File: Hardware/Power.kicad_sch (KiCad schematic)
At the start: 0 parts

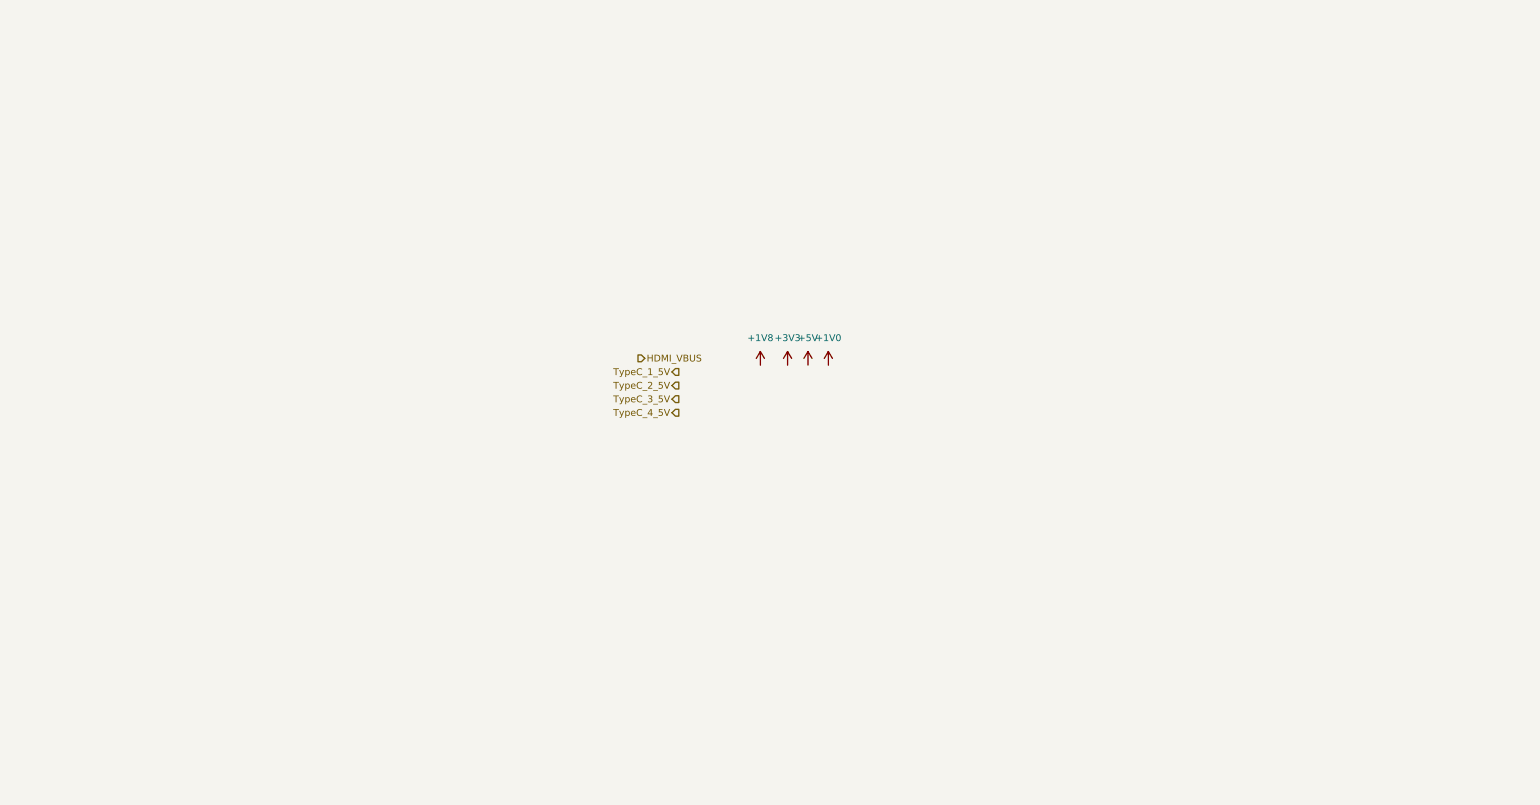
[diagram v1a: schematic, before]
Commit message: 完成除MCU外的设计
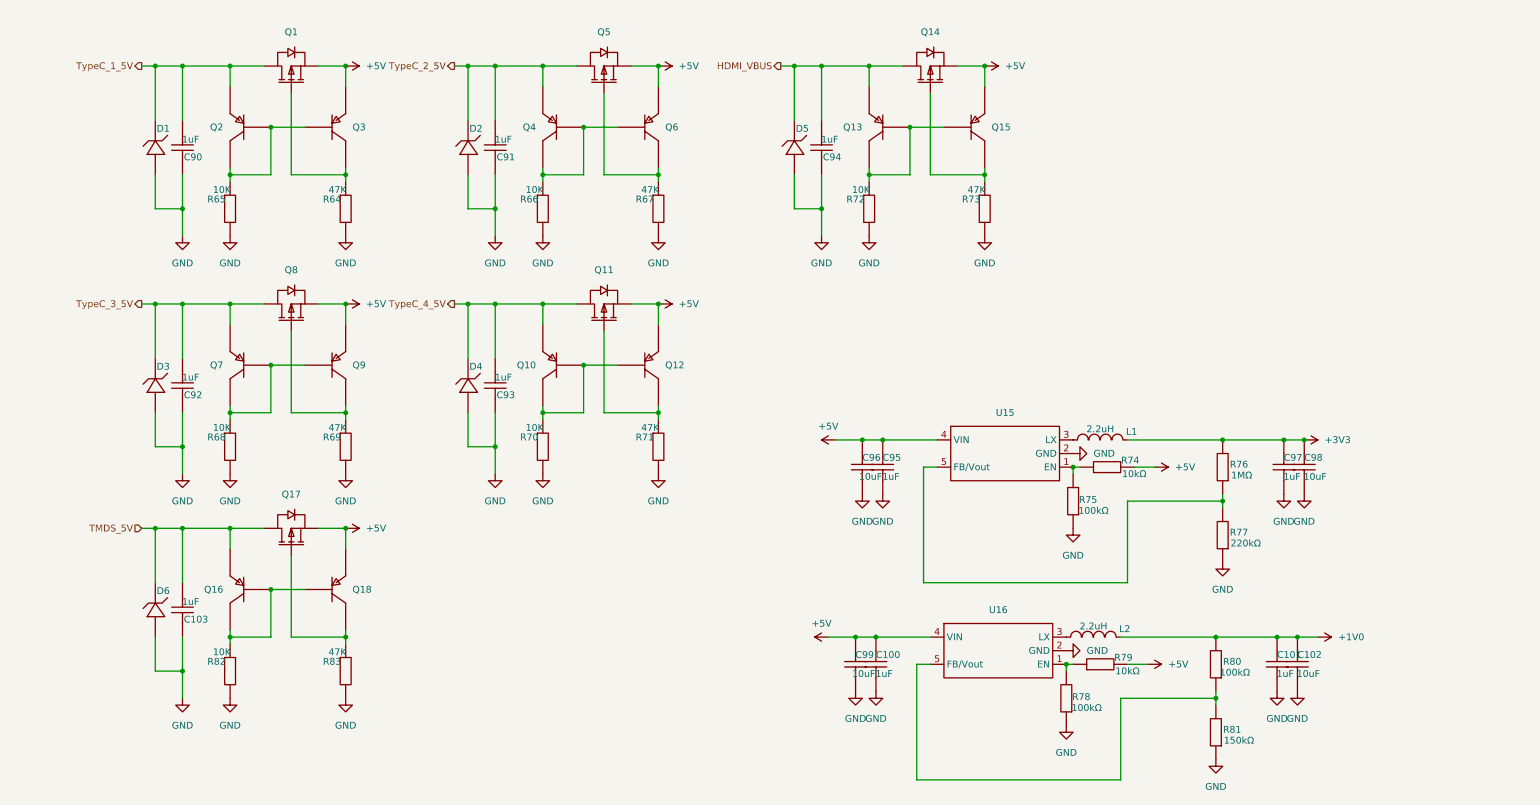
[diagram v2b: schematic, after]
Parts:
- added C100, C101, C103, C90, C91, C92, C93, C94, C95, C97: 1uF, persional_library:C0603, symbol persional_library:C0603
- added C102, C96, C98, C99: 10uF, persional_library:C0603, symbol persional_library:C0603
- added D1, D2, D3, D4, D5, D6: ~, persional_library:SMB_L4.6-W3.6-LS5.3-RD, symbol persional_library:TVS_Diode_SMBJ5.0A
- added L1, L2: 2.2uH, persional_library:IND-SMD_L7.0-W6.6, symbol persional_library:L0630-2.2UH
- added Q1, Q11, Q14, Q17, Q5, Q8: ~, persional_library:SOT-23-3_L2.9-W1.3-P0.95-LS2.4-BR-1, symbol persional_library:MOSFET_DMG2305UX
- added Q10, Q12, Q13, Q15, Q16, Q18, Q2, Q3, Q4, Q6, Q7, Q9: ~, persional_library:SOT-23-3_L2.9-W1.3-P1.90-LS2.4-BR, symbol persional_library:Transistor_PNP_MMBT4403LT1G
- added R64, R67, R69, R71, R73, R83: 47K, persional_library:R0603, symbol persional_library:R0603
- added R65, R66, R68, R70, R72, R82: 10K, persional_library:R0603, symbol persional_library:R0603
- added R74, R79: 10kΩ, persional_library:R0603, symbol persional_library:R0603
- added R75, R78, R80: 100kΩ, persional_library:R0603, symbol persional_library:R0603
- added R76: 1MΩ, persional_library:R0603, symbol persional_library:R0603
- added R77: 220kΩ, persional_library:R0603, symbol persional_library:R0603
- added R81: 150kΩ, persional_library:R0603, symbol persional_library:R0603
- added U15, U16: ~, persional_library:SOT-23-5_L3.0-W1.7-P0.95-LS2.8-BR, symbol persional_library:DCDC-LP3220AB5F
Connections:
- net +1V0: now also C101.2, C102.2, L2.2, R80.2
- net +3V3: now also C97.2, C98.2, L1.2, R76.2
- net +5V: now also C100.2, C95.2, C96.2, C99.2, Q1.2 (S), Q11.2 (S), Q12.2 (E), Q14.2 (S), Q15.2 (E), Q17.2 (S), Q18.2 (E), Q3.2 (E), Q5.2 (S), Q6.2 (E), Q8.2 (S), Q9.2 (E), R74.2, R79.2, U15.4 (VIN), U16.4 (VIN)
- net HDMI_VBUS: now also C94.2, D5.1, Q13.2 (E), Q14.3 (D)
- net TypeC_1_5V: now also C90.2, D1.1, Q1.3 (D), Q2.2 (E)
- net TypeC_2_5V: now also C91.2, D2.1, Q4.2 (E), Q5.3 (D)
- net TypeC_3_5V: now also C92.2, D3.1, Q7.2 (E), Q8.3 (D)
- net TypeC_4_5V: now also C93.2, D4.1, Q10.2 (E), Q11.3 (D)
- new net: Q5.1 (G), Q6.3 (C), R67.1
- new net: Q2.1 (B), Q2.3 (C), Q3.1 (B), R65.1
- new net: Q4.1 (B), Q4.3 (C), Q6.1 (B), R66.1
- new net: Q1.1 (G), Q3.3 (C), R64.1
- new net: Q13.1 (B), Q13.3 (C), Q15.1 (B), R72.1
- new net: Q10.1 (B), Q10.3 (C), Q12.1 (B), R70.1
- new net: R76.1, R77.2, U15.5 (FB/Vout)
- new net: R74.1, R75.2, U15.1 (EN)
- new net: Q16.1 (B), Q16.3 (C), Q18.1 (B), R82.1
- new net: Q11.1 (G), Q12.3 (C), R71.1
- new net: L1.1, U15.3 (LX)
- new net: Q17.1 (G), Q18.3 (C), R83.1
- new net: R78.2, R79.1, U16.1 (EN)
- new net: L2.1, U16.3 (LX)
- new net: R80.1, R81.2, U16.5 (FB/Vout)
- new net: Q14.1 (G), Q15.3 (C), R73.1
- new net: Q7.1 (B), Q7.3 (C), Q9.1 (B), R68.1
- new net: Q8.1 (G), Q9.3 (C), R69.1
- new net GND: C100.1, C101.1, C102.1, C103.1, C90.1, C91.1, C92.1, C93.1, C94.1, C95.1, C96.1, C97.1, C98.1, C99.1, D1.2, D2.2, D3.2, D4.2, D5.2, D6.2, R64.2, R65.2, R66.2, R67.2, R68.2, R69.2, R70.2, R71.2, R72.2, R73.2, R75.1, R77.1, R78.1, R81.1, R82.2, R83.2, U15.2 (GND), U16.2 (GND)
- new net TMDS_5V: C103.2, D6.1, Q16.2 (E), Q17.3 (D)

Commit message: 修改了电源供电部分的内容
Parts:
- removed C102: 10uF, persional_library:C0603, symbol persional_library:C0603
- removed R78, R80: 100kΩ, persional_library:R0603, symbol persional_library:R0603
- removed R79: 10kΩ, persional_library:R0603, symbol persional_library:R0603
- removed R81: 150kΩ, persional_library:R0603, symbol persional_library:R0603
- removed U15, U16: ~, persional_library:SOT-23-5_L3.0-W1.7-P0.95-LS2.8-BR, symbol persional_library:DCDC-LP3220AB5F
- added U15: ~, persional_library:TSOT-23-8_L2.9-W1.6-P0.65-LS2.8-BL, symbol persional_library:DCDC_MP2122AGJ-Z
- added U16: ~, persional_library:SOT-223-4_L6.5-W3.5-P2.30-LS7.0-BR, symbol persional_library:LDO_AMS1117-3.3
- C100, C97: value 1uF -> 10uF
- C101, C95: value 1uF -> 100nF
- R74: value 10kΩ -> 150K
- R75: value 100kΩ -> 150K
- R76: value 1MΩ -> 680K
- R77: value 220kΩ -> 100K
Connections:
- net +1V0: now also C98.2, R77.2; no longer C101.2
- net +3V3: no longer C98.2
- net +5V: now also U15.2 (EN2), U15.4 (EN1), U15.7 (IN), U16.3 (VIN); no longer C100.2, R74.2
- net GND: now also R74.2, R75.2, U15.5 (GND), U16.1 (ADJ(GND)); no longer R75.1, R77.1
- net at R76.1: now also R75.1, U15.8 (FB1); no longer R77.2
- net at R74.1: now also R77.1, U15.1 (FB2); no longer R75.2
- net at L1.1: now also U15.6 (SW1)
- net at L2.1: now also U15.3 (SW2)
- new net +3.3V: C100.2, C101.2, U16.2 (VOUT(TAB)), U16.4 (TAB)

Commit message: complete sch
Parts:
- added F1, F2, F3, F4, F5, F6: ~, persional_library:F1206, symbol persional_library:F1206
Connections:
- net HDMI_VBUS: now also F6.1; no longer C94.2, D5.1, Q13.2 (E), Q14.3 (D)
- net TMDS_5V: now also F3.1; no longer C103.2, D6.1, Q16.2 (E), Q17.3 (D)
- net TypeC_1_5V: now also F1.1; no longer C90.2, D1.1, Q1.3 (D), Q2.2 (E)
- net TypeC_2_5V: now also F5.1; no longer C91.2, D2.1, Q4.2 (E), Q5.3 (D)
- net TypeC_3_5V: now also F2.1; no longer C92.2, D3.1, Q7.2 (E), Q8.3 (D)
- net TypeC_4_5V: now also F4.1; no longer C93.2, D4.1, Q10.2 (E), Q11.3 (D)
- new net: C90.2, D1.1, F1.2, Q1.3 (D), Q2.2 (E)
- new net: C94.2, D5.1, F6.2, Q13.2 (E), Q14.3 (D)
- new net: C91.2, D2.1, F5.2, Q4.2 (E), Q5.3 (D)
- new net: C103.2, D6.1, F3.2, Q16.2 (E), Q17.3 (D)
- new net: C92.2, D3.1, F2.2, Q7.2 (E), Q8.3 (D)
- new net: C93.2, D4.1, F4.2, Q10.2 (E), Q11.3 (D)
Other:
- moved on the sheet: C91, C93, C94, D2, D4, D5, Q10, Q11, Q12, Q13, Q14, Q15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

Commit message: 开始PCB布局
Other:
- note added: "DCDC 3v3 1v0"
- note added: "LDO 3v3"
- note added: "计算公式:0.6*(1+R1/R2) 上路输出为3.32v 下路为1.0v"
- note added: "负责MCU供电"
- note added: "防浪涌电路"
- moved on the sheet: C100, C101, C103, C90, C91, C92, C93, C94, C95, C96, C97, C98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
